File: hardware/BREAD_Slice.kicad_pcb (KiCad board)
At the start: 2 copper layers, 70 x 100 mm, 46 parts, among them J1 I2C_01x04, J2 Conn_01x10_Female, J3 Screw_Terminal_01x04, J4 Screw_Terminal_01x03, J5 Screw_Terminal_01x03, J6 Screw_Terminal_01x03, J7 Screw_Terminal_01x03, K1 G5Q-1, K2 G5Q-1, K3 G5Q-1, K4 G5Q-1, U2 TCMT1100, U3 TCMT1100, U4 TCMT1100, U5 TCMT1100

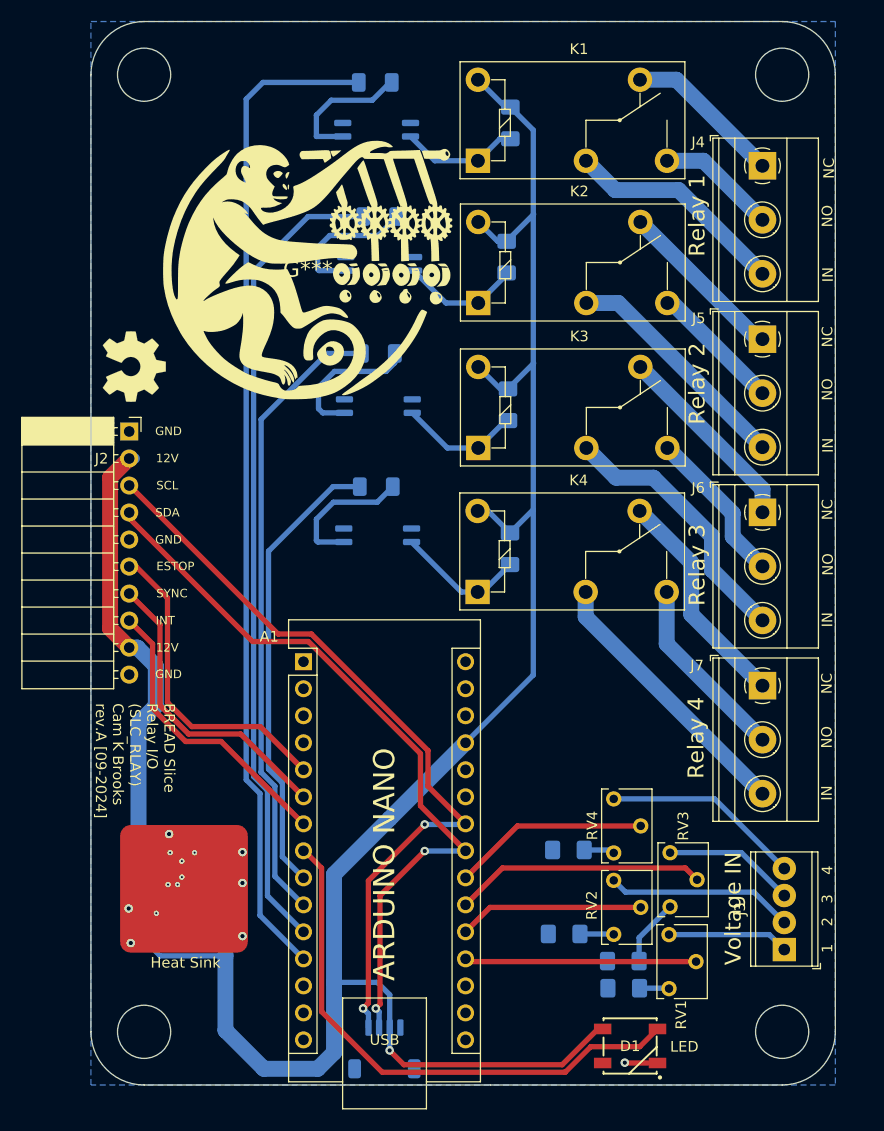
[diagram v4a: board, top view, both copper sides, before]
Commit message: update to use latest kmlib; needs revision for connectors and ground inputs on analog inputs
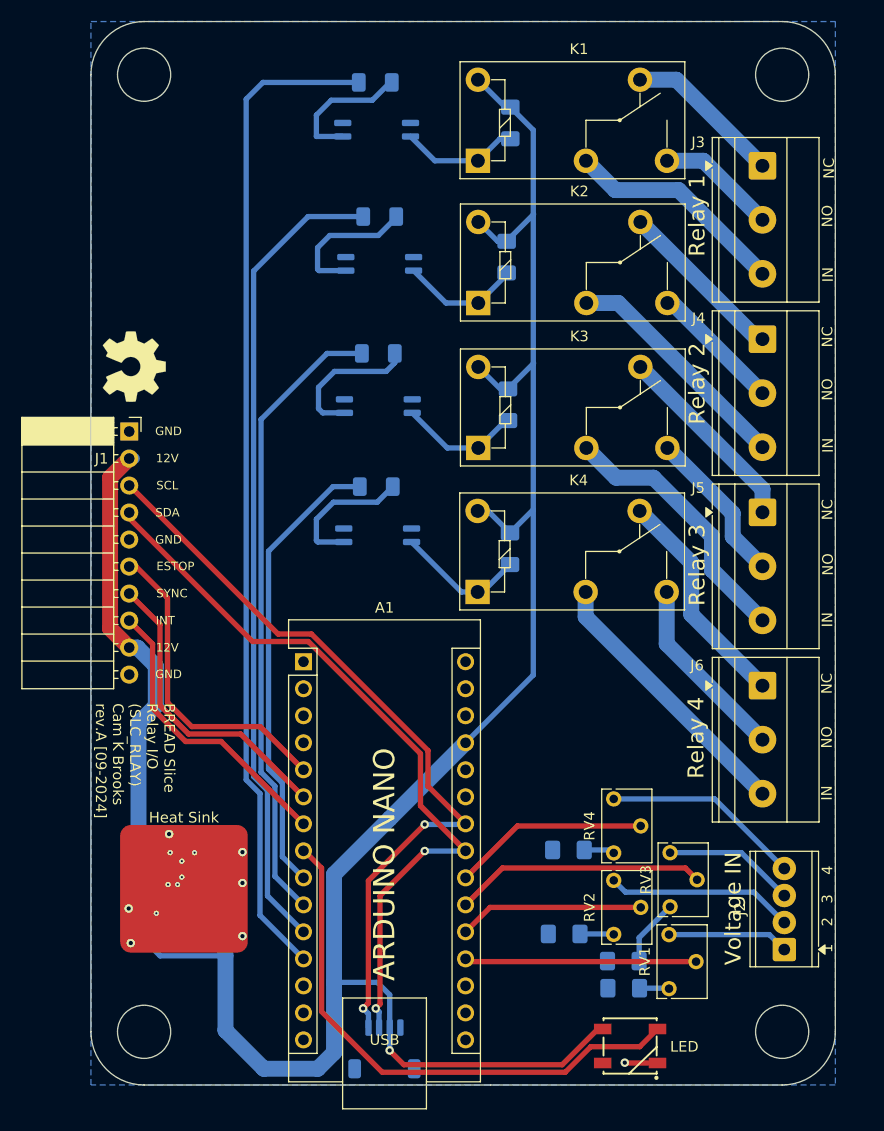
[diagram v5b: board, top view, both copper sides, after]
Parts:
- removed G***: LOGO, LOGO
- A1: footprint Module:Arduino_Nano -> KMLib_Boards_Modules:Arduino_Nano
- D1: footprint SparkFun-LED:WS2812-5050-4PIN -> KMLib_IC_SMD:WS2812-5050-4PIN
- HS1: footprint KML-Custom:Thermal Pad -> KMLib_Mounting:Thermal Pad
- U1: footprint Package_TO_SOT_SMD:TSOT-23-6 -> KMLib_IC_SMD:SOIC_05WU-7_DIO
- renumbered J2 to J1, J3 to J2, J4 to J3, J5 to J4, J6 to J5, J7 to J6
